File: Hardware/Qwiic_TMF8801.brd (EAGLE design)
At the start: 25.4 x 25.4 mm, 49 parts, among them J1 QWIIC_RIGHT_ANGLE, J2 QWIIC_RIGHT_ANGLE, U1 TMF8801

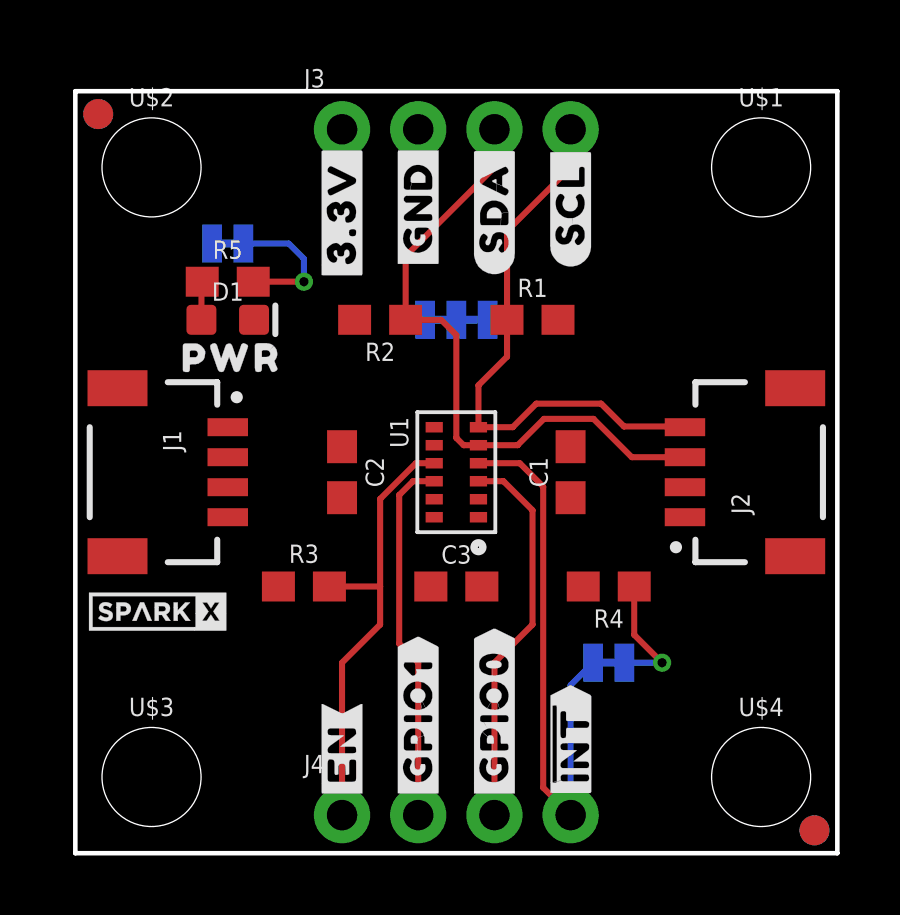
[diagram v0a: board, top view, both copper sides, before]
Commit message: Layout changes
Changed board layout per Nathan's feedback.
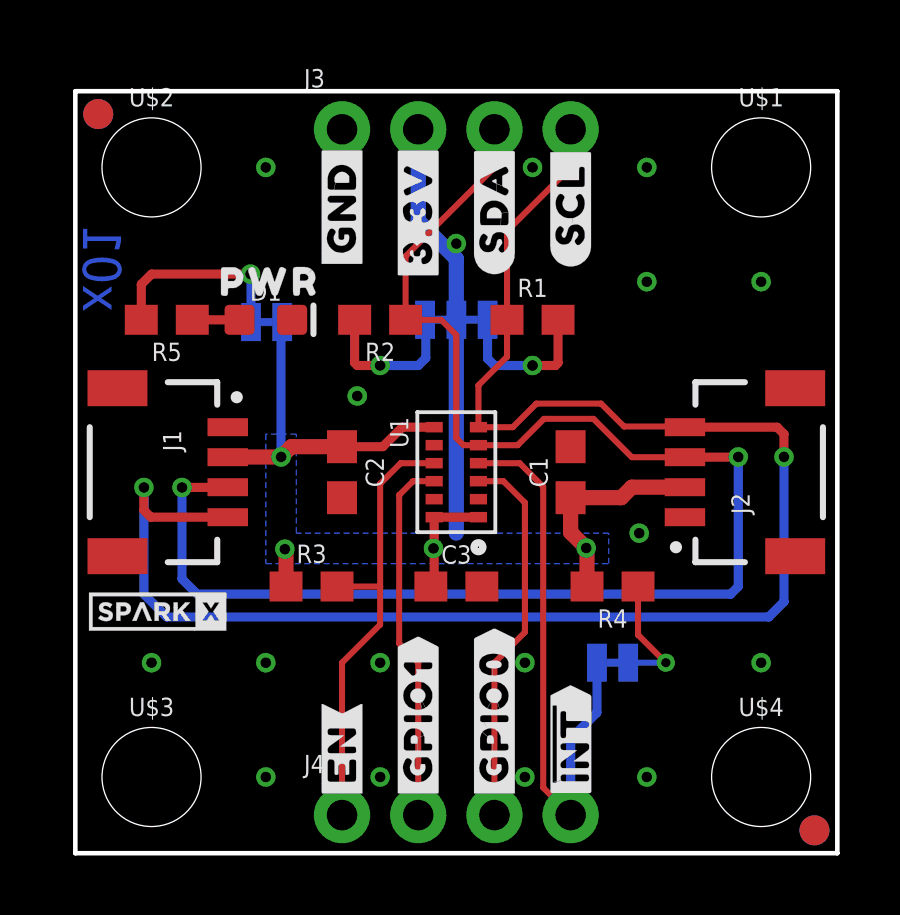
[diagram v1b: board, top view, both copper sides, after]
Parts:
- removed FRAME1: FRAME-LETTERNO_PACKAGE, SparkFun-Aesthetics:DUMMY
- moved U$12 3.56 mm to (17.8, 8.26)
- moved JP3 2.92 mm to (6.38, 17.7), turned to 180 degrees
- moved U$29 2.86 mm to (6.32, 16.0)
- moved U$30 2.84 mm to (6.48, 19.1)
- moved U$17 2.54 mm to (11.4, 18.9)
- moved U$18 2.54 mm to (8.89, 19.3)
- moved U$5 2.54 mm to (11.4, 18.9)
- moved U$7 2.54 mm to (8.89, 19.3)
- moved R5 2.40 mm to (3.05, 17.8), turned to 180 degrees
- moved D1 1.27 mm to (6.35, 17.8)
- moved R3 0.25 mm to (7.87, 8.89)
- moved JP2 0.13 mm to (17.9, 6.35)
- moved R4 0.13 mm to (17.9, 8.89)
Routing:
- net SCL: track 18.7 -> 56.8 mm, vias 0 -> 2
- net 3.3V: track 0.00 -> 37.9 mm, vias 0 -> 4
- net SDA: track 21.5 -> 51.1 mm, vias 0 -> 2
- net N$3: track 0.00 -> 5.23 mm, vias 0 -> 1
- net N$2: track 0.00 -> 5.21 mm, vias 0 -> 1
- net N$4: track 4.68 -> 6.57 mm
- added copper zone on layer 16, net 3.3V
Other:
- board text added: "x01"

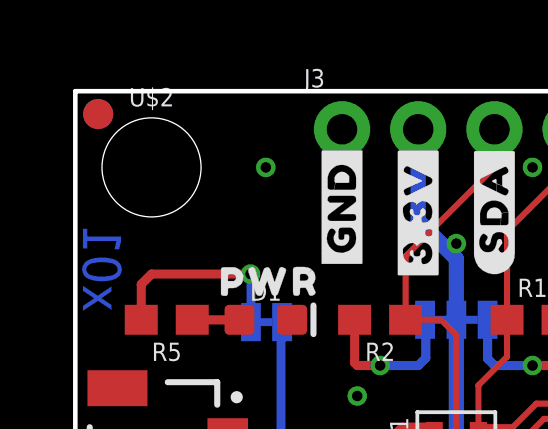
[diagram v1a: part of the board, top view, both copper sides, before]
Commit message: Added missing frame to schematic; removed extra fiducial
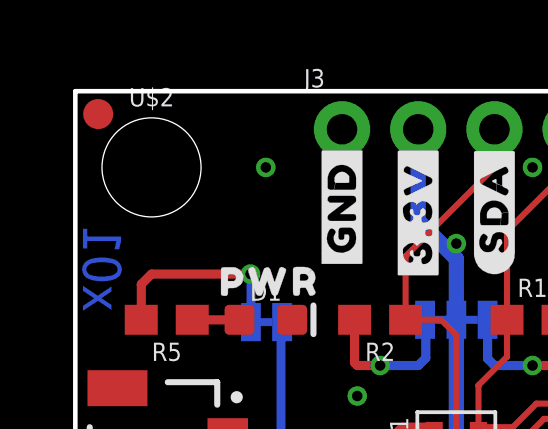
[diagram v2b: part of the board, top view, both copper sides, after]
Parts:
- removed FD2: FIDUCIAL1X2, SparkFun-Aesthetics:FIDUCIAL-1X2
- added FRAME1: FRAME-LETTERNO_PACKAGE, SparkFun-Aesthetics:DUMMY
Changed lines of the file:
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@@
 </element>
 <element name="FD1" library="SparkFun-Aesthetics" package="FIDUCIAL-1X2" value="FIDUCIAL1X2" x="0.762" y="24.638" smashed="yes"/>
-<element name="FD2" library="SparkFun-Aesthetics" package="FIDUCIAL-1X2" value="FIDUCIAL1X2" x="0.762" y="24.638" smashed="yes" rot="MR0"/>
 <element name="FD3" library="SparkFun-Aesthetics" package="FIDUCIAL-1X2" value="FIDUCIAL1X2" x="24.638" y="0.762" smashed="yes"/>
 <element name="FD4" library="SparkFun-Aesthetics" package="FIDUCIAL-1X2" value="FIDUCIAL1X2" x="24.638" y="0.762" smashed="yes" rot="MR0"/>
@@
 <element name="U$30" library="output" package="PWR2" value="" x="6.477" y="19.05" smashed="yes"/>
 <element name="U$12" library="output" package="#INT0" value="" x="17.78" y="8.255" smashed="yes" rot="MR0"/>
+<element name="FRAME1" library="SparkFun-Aesthetics" package="DUMMY" value="FRAME-LETTERNO_PACKAGE" x="-0.254" y="-0.508" smashed="yes">
+<attribute name="DESIGNER" value="Ricardo R" x="-0.254" y="-0.508" size="1.778" layer="27" display="off"/>
+<attribute name="VERSION" value="v01" x="-0.254" y="-0.508" size="1.778" layer="27" display="off"/>
+</element>
 </elements>
 <signals>
